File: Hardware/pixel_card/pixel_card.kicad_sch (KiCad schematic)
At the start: 89 parts, among them J2 DEBUG, SW1 UP, SW2 DOWN, SW3 LEFT, SW4 RIGTH, SW5 ACTION, U1 IS31FL3731-QF, U2 ATtiny1616-M, U3 AP2127K-3.0, U4 XC6210B182MR-G, U5 TPS2116DRLR

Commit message: Coin cell battery design, end routing power mux
1. Designing circuit for double CR2032 batteries with additional
   capacitors to help during huge current
2. Added voltage divider for power mux (2x 50Ohm should always give
   voltage above 1V Vref of power mux)
3. Started cleaning schematic
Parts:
- added BT1, BT2: 3002, 3002:BAT_3002, symbol Keystone 3002:3002
- added C10, C11: 330uF, Capacitor_SMD:C_1206_3216Metric, symbol Device:C_Small
- added R7, R8: 50R, Resistor_SMD:R_0603_1608Metric, symbol Device:R
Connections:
- net +5V: now also R7.1
- net GND: now also BT2.N, C10.2, C11.2
- net VBATT: now also BT1.P1, C10.1, C11.1
- net at U5.4 (PR1): now also R7.2, R8.1
- new net: BT1.N, BT2.P1
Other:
- moved on the sheet: C1, C2, C3, R4

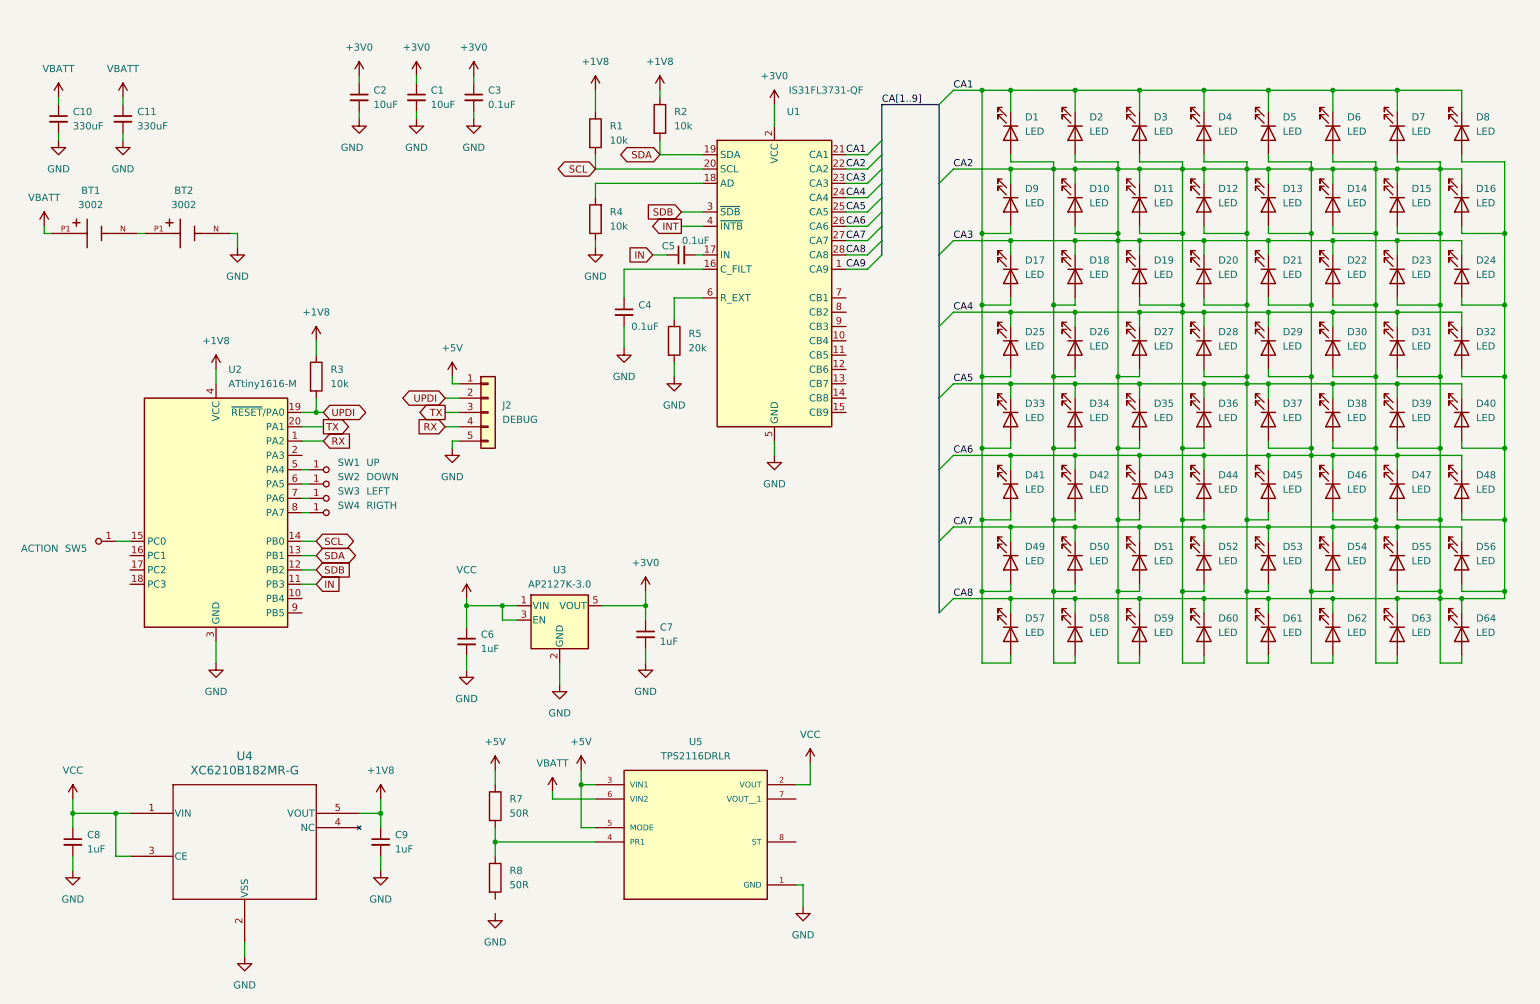
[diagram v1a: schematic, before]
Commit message: Finishing schematic
1. Cleaning up schematic
2. Running and fixing erros from electrical rule check
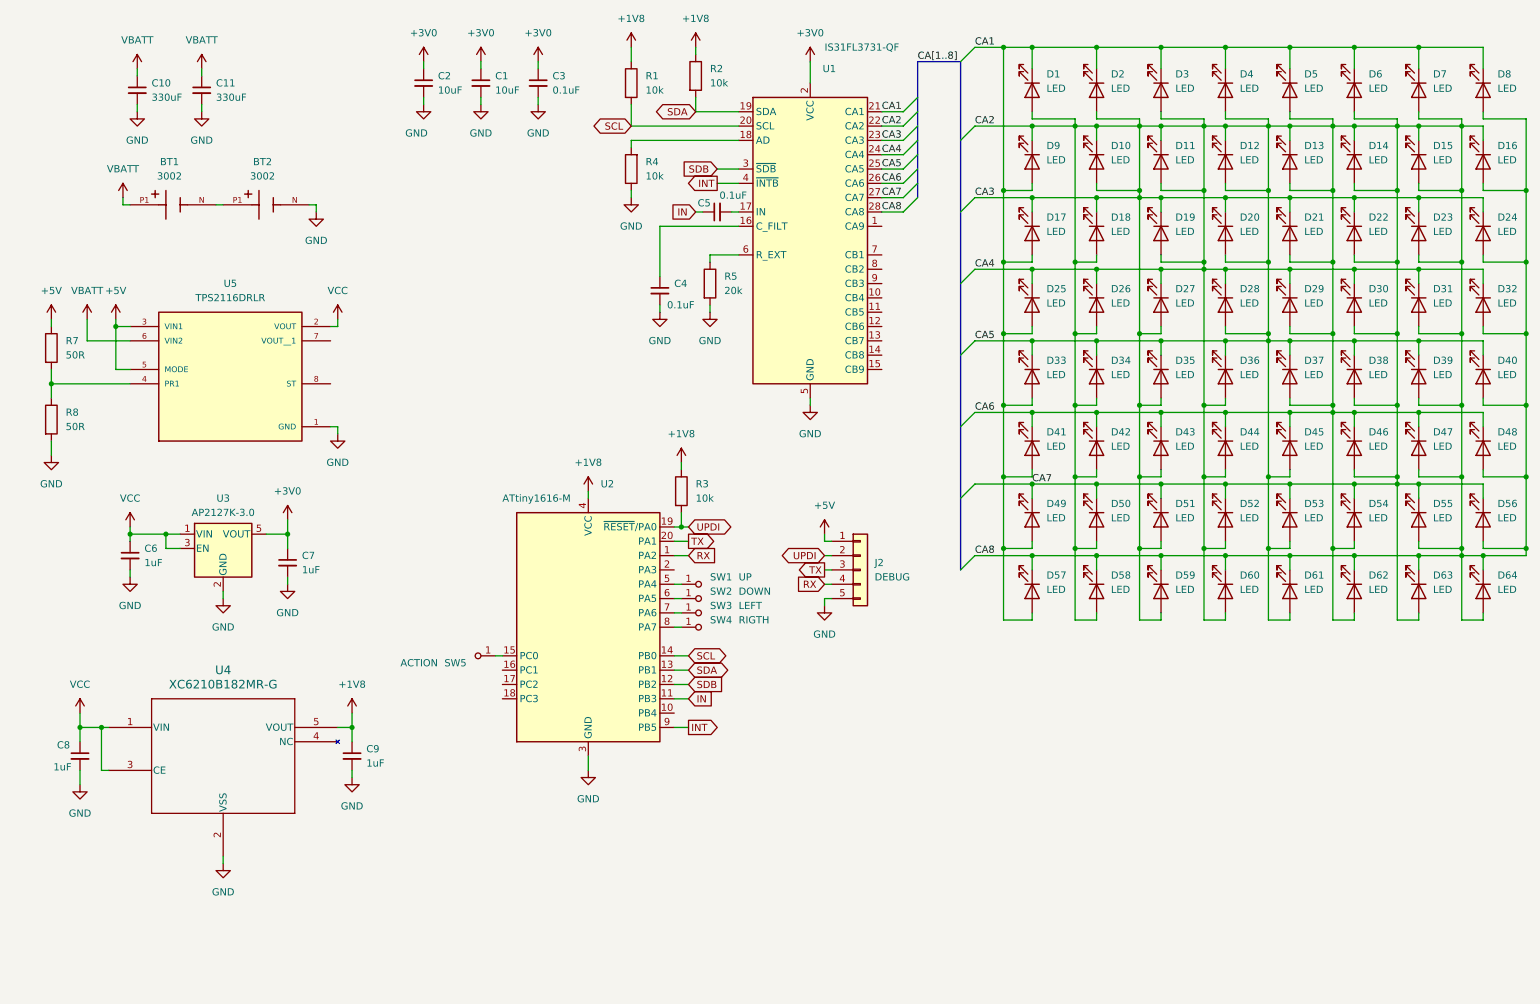
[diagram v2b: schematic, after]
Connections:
- net GND: now also R8.2
- net INT: now also U2.9 (PB5)
- net CA9: no longer names the net of U1.1 (CA9)
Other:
- moved on the sheet: BT1, BT2, C1, C10, C11, C2, C3, C4, C5, C6, C7, C8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

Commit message: Fixing schematic and mocing to pcb
1. Adding not-connected pin symbols
2. Adding footprints
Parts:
- BT1, BT2: footprint 3002:BAT_3002 -> Keystone 3002:BAT_3002
- C1, C2, C3, C4, C5, C6, C7, C8, C9: footprint (none) -> Capacitor_SMD:C_0603_1608Metric
- D1, D10, D11, D12, D13, D14, D15, D16, D17, D18, D19, D2, D20, D21, D22, D23, D24, D25, D26, D27, D28, D29, D3, D30, D31, D32, D33, D34, D35, D36, D37, D38, D39, D4, D40, D41, D42, D43, D44, D45, D46, D47, D48, D49, D5, D50, D51, D52, D53, D54, D55, D56, D57, D58, D59, D6, D60, D61, D62, D63, D64, D7, D8, D9: footprint (none) -> LED_SMD:LED_0603_1608Metric
- U4: footprint SOT-25_TOR -> XC6210B182MR-G:SOT-25_TOR
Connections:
- no-connect marks 0 -> 17
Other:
- moved on the sheet: BT2
